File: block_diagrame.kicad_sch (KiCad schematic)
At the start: 0 parts

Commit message: Update v2 schematics + PCB: impedance profiles, design rules, sheet fixes
- pro: copper/track widths, microvias, 40/50 OHM + DIFF 85/90/100 tuning profiles
- dru/pcb: updated constraints and layout
- sheets: RK3576, RP2350A, Fixtures, MIPI, PCIe, HDMI, LPDDR5, UFS/eMMC, OLED, block diagram
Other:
- sheet OLED Screen ports: added OLED Display; removed none
- sheet RP2350A MCU ports: added OLED Display; removed none
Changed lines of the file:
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@@
 	(generator_version "10.0")
 	(paper "A4")
+	(bus
+		(pts
+			(xy 129.54 87.63) (xy 137.16 87.63)
+		)
+		(stroke
+			(width 0)
+			(type default)
+		)
+	)
+	(bus
+		(pts
+			(xy 137.16 68.58) (xy 137.16 87.63)
+		)
+		(stroke
+			(width 0)
+			(type default)
+		)
+	)
+	(bus
+		(pts
+			(xy 147.32 68.58) (xy 137.16 68.58)
+		)
+		(stroke
+			(width 0)
+			(type default)
+		)
+	)
 	(image
 		(at 309.88 135.89)
@@
 			)
 		)
+		(pin "OLED Display" bidirectional
+			(at 147.32 68.58 180)
+			(effects
+				(font
+					(size 1.27 1.27)
+				)
+				(justify left)
+			)
+		)
 		(instances
 			(project "RK3576 SBCv2"
@@
 			)
 		)
+		(pin "OLED Display" bidirectional
+			(at 129.9 87.63 0)
+			(effects
+				(font
+					(size 1.27 1.27)
+				)
+				(justify right)
+			)
+		)

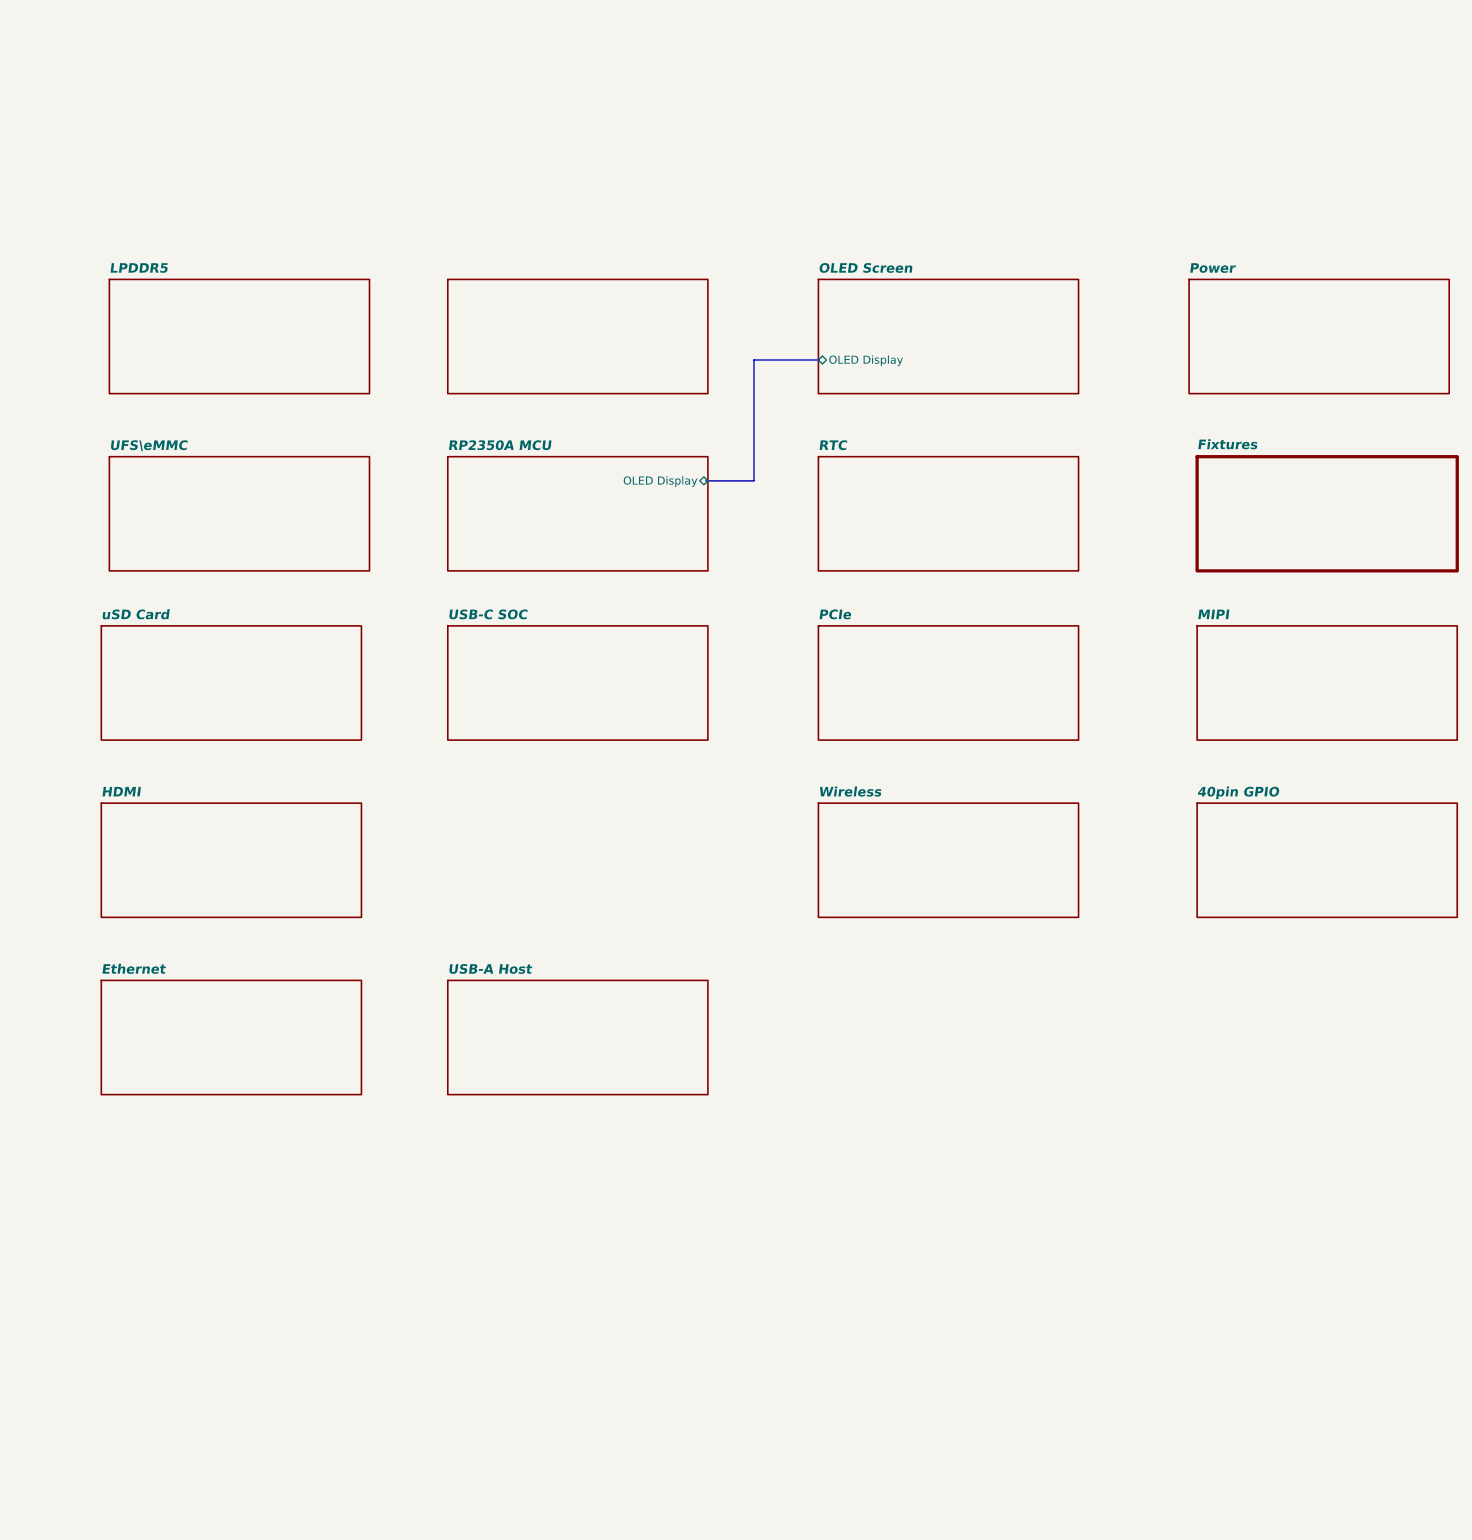
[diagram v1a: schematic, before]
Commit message: block diagrame with Hierarchical labels and NVMe SSD footprint
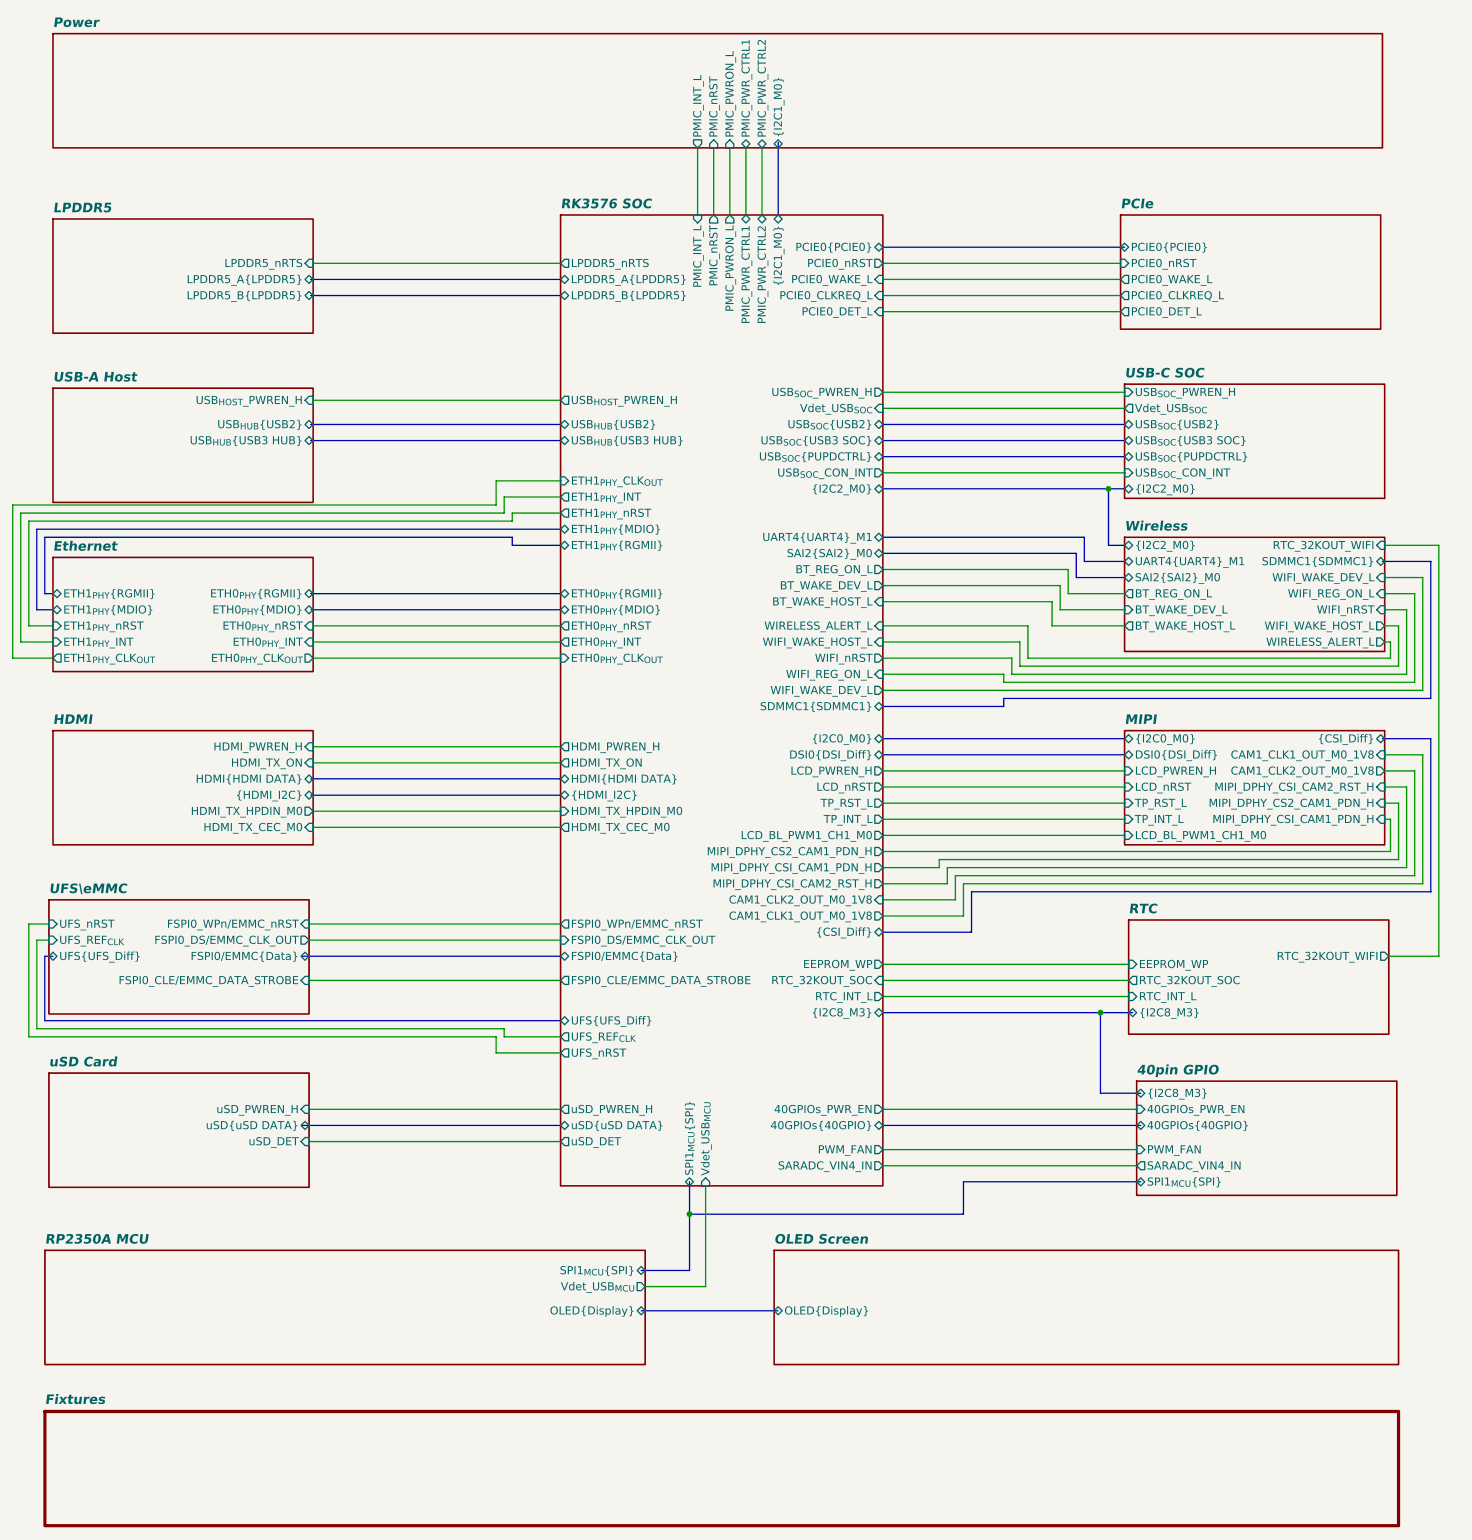
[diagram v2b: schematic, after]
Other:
- sheet 40pin GPIO ports: added 40GPIOs_PWR_EN, 40GPIOs{40GPIO}, PWM_FAN, SARADC_VIN4_IN, SPI1_{MCU}{SPI}, {I2C8_M3}; removed none
- sheet Ethernet ports: added ETH0_{PHY}_CLK_{OUT}, ETH0_{PHY}_INT, ETH0_{PHY}_nRST, ETH0_{PHY}{MDIO}, ETH0_{PHY}{RGMII}, ETH1_{PHY}_CLK_{OUT}, ETH1_{PHY}_INT, ETH1_{PHY}_nRST, ETH1_{PHY}{MDIO}, ETH1_{PHY}{RGMII}; removed none
- sheet HDMI ports: added HDMI_PWREN_H, HDMI_TX_CEC_M0, HDMI_TX_HPDIN_M0, HDMI_TX_ON, HDMI{HDMI DATA}, {HDMI_I2C}; removed none
- sheet LPDDR5 ports: added LPDDR5_A{LPDDR5}, LPDDR5_B{LPDDR5}, LPDDR5_nRTS; removed none
- sheet MIPI ports: added CAM1_CLK1_OUT_M0_1V8, CAM1_CLK2_OUT_M0_1V8, DSI0{DSI_Diff}, LCD_BL_PWM1_CH1_M0, LCD_PWREN_H, LCD_nRST, MIPI_DPHY_CS2_CAM1_PDN_H, MIPI_DPHY_CSI_CAM1_PDN_H, MIPI_DPHY_CSI_CAM2_RST_H, TP_INT_L, TP_RST_L, {CSI_Diff}, {I2C0_M0}; removed none
- sheet OLED Screen ports: added OLED{Display}; removed OLED Display
- sheet PCIe ports: added PCIE0_CLKREQ_L, PCIE0_DET_L, PCIE0_WAKE_L, PCIE0_nRST, PCIE0{PCIE0}; removed none
- sheet Power ports: added PMIC_INT_L, PMIC_PWRON_L, PMIC_PWR_CTRL1, PMIC_PWR_CTRL2, PMIC_nRST, {I2C1_M0}; removed none
- sheet RK3576 SOC ports: added 40GPIOs_PWR_EN, 40GPIOs{40GPIO}, BT_REG_ON_L, BT_WAKE_DEV_L, BT_WAKE_HOST_L, CAM1_CLK1_OUT_M0_1V8, CAM1_CLK2_OUT_M0_1V8, DSI0{DSI_Diff}, EEPROM_WP, ETH0_{PHY}_CLK_{OUT}, ETH0_{PHY}_INT, ETH0_{PHY}_nRST, ETH0_{PHY}{MDIO}, ETH0_{PHY}{RGMII}, ETH1_{PHY}_CLK_{OUT}, ETH1_{PHY}_INT, ETH1_{PHY}_nRST, ETH1_{PHY}{MDIO}, ETH1_{PHY}{RGMII}, FSPI0_CLE/EMMC_DATA_STROBE, FSPI0_DS/EMMC_CLK_OUT, FSPI0_WPn/EMMC_nRST, FSPI0/EMMC{Data}, HDMI_PWREN_H, HDMI_TX_CEC_M0, HDMI_TX_HPDIN_M0, HDMI_TX_ON, HDMI{HDMI DATA}, LCD_BL_PWM1_CH1_M0, LCD_PWREN_H, LCD_nRST, LPDDR5_A{LPDDR5}, LPDDR5_B{LPDDR5}, LPDDR5_nRTS, MIPI_DPHY_CS2_CAM1_PDN_H, MIPI_DPHY_CSI_CAM1_PDN_H, MIPI_DPHY_CSI_CAM2_RST_H, PCIE0_CLKREQ_L, PCIE0_DET_L, PCIE0_WAKE_L, PCIE0_nRST, PCIE0{PCIE0}, PMIC_INT_L, PMIC_PWRON_L, PMIC_PWR_CTRL1, PMIC_PWR_CTRL2, PMIC_nRST, PWM_FAN, RTC_32KOUT_SOC, RTC_INT_L, SAI2{SAI2}_M0, SARADC_VIN4_IN, SDMMC1{SDMMC1}, SPI1_{MCU}{SPI}, TP_INT_L, TP_RST_L, UART4{UART4}_M1, UFS_REF_{CLK}, UFS_nRST, UFS{UFS_Diff}, USB_{HOST}_PWREN_H, USB_{HUB}{USB2}, USB_{HUB}{USB3 HUB}, USB_{SOC}_CON_INT, USB_{SOC}_PWREN_H, USB_{SOC}{PUPDCTRL}, USB_{SOC}{USB2}, USB_{SOC}{USB3 SOC}, Vdet_USB_{MCU}, Vdet_USB_{SOC}, WIFI_REG_ON_L, WIFI_WAKE_DEV_L, WIFI_WAKE_HOST_L, WIFI_nRST, WIRELESS_ALERT_L, uSD_DET, uSD_PWREN_H, uSD{uSD DATA}, {CSI_Diff}, {HDMI_I2C}, {I2C0_M0}, {I2C1_M0}, {I2C2_M0}, {I2C8_M3}; removed none
- sheet RP2350A MCU ports: added OLED{Display}, SPI1_{MCU}{SPI}, Vdet_USB_{MCU}; removed OLED Display
- sheet RTC ports: added EEPROM_WP, RTC_32KOUT_SOC, RTC_32KOUT_WIFI, RTC_INT_L, {I2C8_M3}; removed none
- sheet UFS\eMMC ports: added FSPI0_CLE/EMMC_DATA_STROBE, FSPI0_DS/EMMC_CLK_OUT, FSPI0_WPn/EMMC_nRST, FSPI0/EMMC{Data}, UFS_REF_{CLK}, UFS_nRST, UFS{UFS_Diff}; removed none
- sheet USB-A Host ports: added USB_{HOST}_PWREN_H, USB_{HUB}{USB2}, USB_{HUB}{USB3 HUB}; removed none
- sheet USB-C SOC ports: added USB_{SOC}_CON_INT, USB_{SOC}_PWREN_H, USB_{SOC}{PUPDCTRL}, USB_{SOC}{USB2}, USB_{SOC}{USB3 SOC}, Vdet_USB_{SOC}, {I2C2_M0}; removed none
- sheet Wireless ports: added BT_REG_ON_L, BT_WAKE_DEV_L, BT_WAKE_HOST_L, RTC_32KOUT_WIFI, SAI2{SAI2}_M0, SDMMC1{SDMMC1}, UART4{UART4}_M1, WIFI_REG_ON_L, WIFI_WAKE_DEV_L, WIFI_WAKE_HOST_L, WIFI_nRST, WIRELESS_ALERT_L, {I2C2_M0}; removed none
- sheet uSD Card ports: added uSD_DET, uSD_PWREN_H, uSD{uSD DATA}; removed none
